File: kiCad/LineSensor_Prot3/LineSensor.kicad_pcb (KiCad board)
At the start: 2 copper layers, 146 parts, among them J1 Conn_01x04_Socket, J2 Conn_01x02_Socket, Q1 Q_Photo_NPN, Q10 Q_Photo_NPN, Q11 Q_Photo_NPN, Q12 Q_Photo_NPN, Q13 Q_Photo_NPN, Q14 Q_Photo_NPN, Q15 Q_Photo_NPN, Q16 Q_Photo_NPN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

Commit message: 円とセンサーの配置ずれるな..11/9
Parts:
- moved Q12 280.8 mm to (82.1, 177.8), turned to 157.5 degrees
- moved Q11 274.3 mm to (92.5, 162.2), turned to 135 degrees
- moved Q10 262.0 mm to (108.1, 151.8), turned to 112.5 degrees
- moved Q9 245.5 mm to (126.5, 148.2), turned to 90 degrees
- moved Q2 243.9 mm to (82.0, 214.5), turned to -157.5 degrees
- moved Q13 227.5 mm to (126.5, 244.2), turned to -90 degrees
- moved Q3 226.4 mm to (92.4, 230.1), turned to -135 degrees
- moved Q8 226.2 mm to (144.8, 151.8), turned to 67.5 degrees
- moved Q14 212.3 mm to (144.8, 240.5), turned to -67.5 degrees
- moved Q7 207.0 mm to (160.4, 162.2), turned to 45 degrees
- moved Q4 204.7 mm to (108.0, 240.5), turned to -112.5 degrees
- moved Q15 197.6 mm to (160.4, 230.1), turned to -45 degrees
- moved Q6 190.1 mm to (170.8, 177.8), turned to 22.5 degrees
- moved Q16 189.9 mm to (170.8, 214.5), turned to -22.5 degrees
- moved Q5 179.8 mm to (174.4, 196.2)
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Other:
- board text added: "ココ⇒"

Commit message: センサーフットプリント調整.11.9
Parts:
- removed D17: D, Diode_THT:D_DO-201AD_P12.70mm_Horizontal
- moved A1 230.2 mm to (427.4, 2.23)
- moved C10 230.2 mm to (428.2, 27.3)
- moved C2 230.2 mm to (419.7, 36.4)
- moved C3 230.2 mm to (410.3, 36.7)
- moved C4 230.2 mm to (428.2, 51.6)
- moved C5 230.2 mm to (428.2, 47.6)
- moved C7 230.2 mm to (428.2, 39.5)
- moved C8 230.2 mm to (428.2, 35.4)
- moved C9 230.2 mm to (428.2, 31.4)
- moved D18 230.2 mm to (352.4, -10.7)
- moved D19 230.2 mm to (349.8, -10.7)
- moved D20 230.2 mm to (347.2, -10.7)
- moved D21 230.2 mm to (344.6, -10.7)
- moved D22 230.2 mm to (342.0, -10.7)
- moved D23 230.2 mm to (339.5, -10.7)
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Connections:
- RV1 pad 2: Net-(U3A--) -> Net-(U3A-+)
- RV2 pad 2: Net-(U5A--) -> Net-(U5A-+)
- RV4 pad 2: Net-(U1A--) -> Net-(U1A-+)
- U1 pad 2: Net-(U1A--) -> Net-(Q13-E)
- U1 pad 3: Net-(Q13-E) -> Net-(U1A-+)
- U1 pad 5: Net-(Q14-E) -> Net-(U1A-+)
- U1 pad 6: Net-(U1A--) -> Net-(Q14-E)
- U2 pad 2: Net-(U1A--) -> Net-(Q15-E)
- U2 pad 3: Net-(Q15-E) -> Net-(U1A-+)
- U2 pad 5: Net-(Q16-E) -> Net-(U1A-+)
- U2 pad 6: Net-(U1A--) -> Net-(Q16-E)
- U3 pad 2: Net-(U3A--) -> Net-(Q1-E)
- U3 pad 3: Net-(Q1-E) -> Net-(U3A-+)
- U3 pad 5: Net-(Q2-E) -> Net-(U3A-+)
- U3 pad 6: Net-(U3A--) -> Net-(Q2-E)
- U4 pad 2: Net-(U3A--) -> Net-(Q3-E)
- U4 pad 3: Net-(Q3-E) -> Net-(U3A-+)
- U4 pad 5: Net-(Q4-E) -> Net-(U3A-+)
- U4 pad 6: Net-(U3A--) -> Net-(Q4-E)
- U5 pad 2: Net-(U5A--) -> Net-(Q12-E)
- U5 pad 3: Net-(Q12-E) -> Net-(U5A-+)
- U5 pad 5: Net-(Q11-E) -> Net-(U5A-+)
- U5 pad 6: Net-(U5A--) -> Net-(Q11-E)
- U6 pad 2: Net-(U5A--) -> Net-(Q10-E)
- U6 pad 3: Net-(Q10-E) -> Net-(U5A-+)
- U6 pad 5: Net-(Q9-E) -> Net-(U5A-+)
- U6 pad 6: Net-(U5A--) -> Net-(Q9-E)
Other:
- board text added: "300,200"

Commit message: 修学旅行行き新幹線
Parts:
- moved R67 479.4 mm to (63.9, 183.9)
- moved R12 477.8 mm to (49.9, 127.9)
- moved R13 477.8 mm to (49.9, 130.4)
- moved R14 477.8 mm to (49.9, 132.9)
- moved R15 477.8 mm to (49.9, 135.5)
- moved R16 477.8 mm to (49.9, 138.0)
- moved R17 477.8 mm to (49.9, 140.5)
- moved R18 477.8 mm to (49.9, 143.0)
- moved R19 477.8 mm to (49.9, 145.5)
- moved R20 477.8 mm to (49.9, 148.0)
- moved R21 477.8 mm to (49.9, 150.5)
- moved R22 477.8 mm to (49.9, 153.0)
- moved R45 477.8 mm to (63.0, 127.9)
- moved R46 477.8 mm to (63.0, 130.4)
- moved R47 477.8 mm to (63.0, 132.9)
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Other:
- board text removed: "300,200"
- board text removed: "ココ⇒"

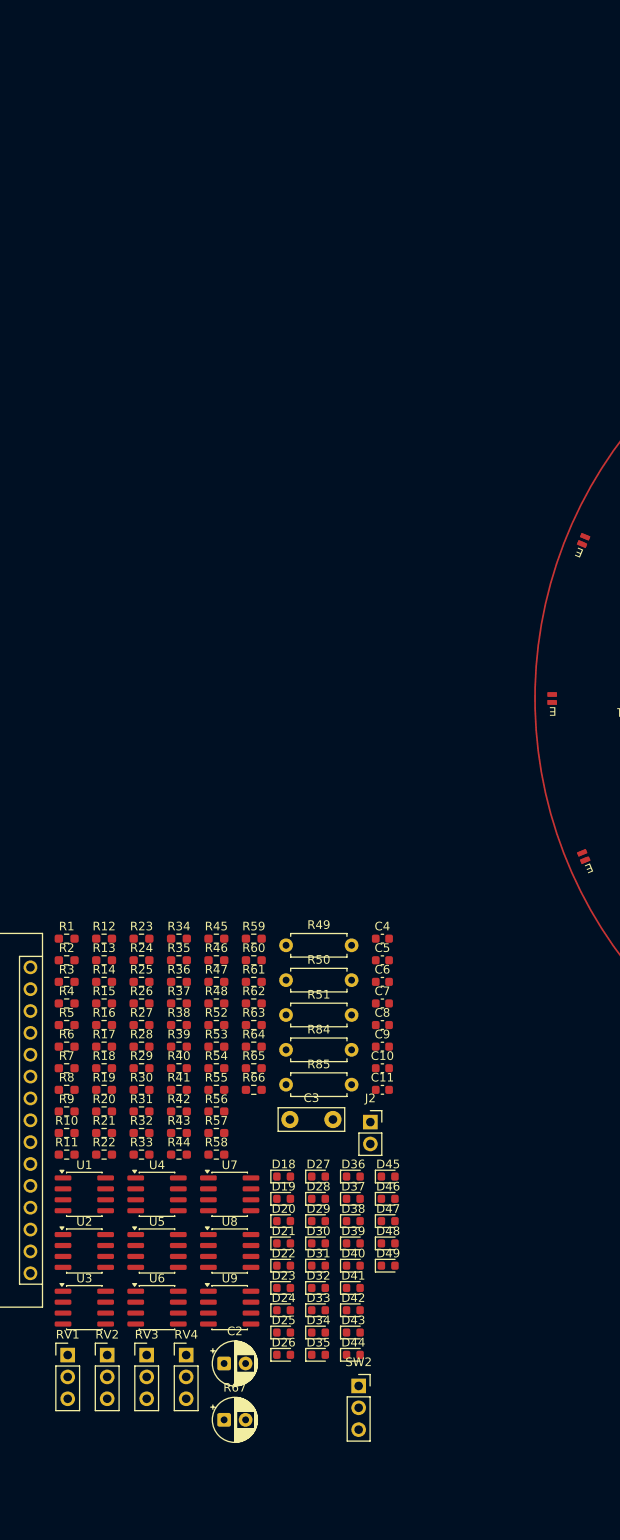
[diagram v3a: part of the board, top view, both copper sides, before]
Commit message: 11/1夜_LED配置まで
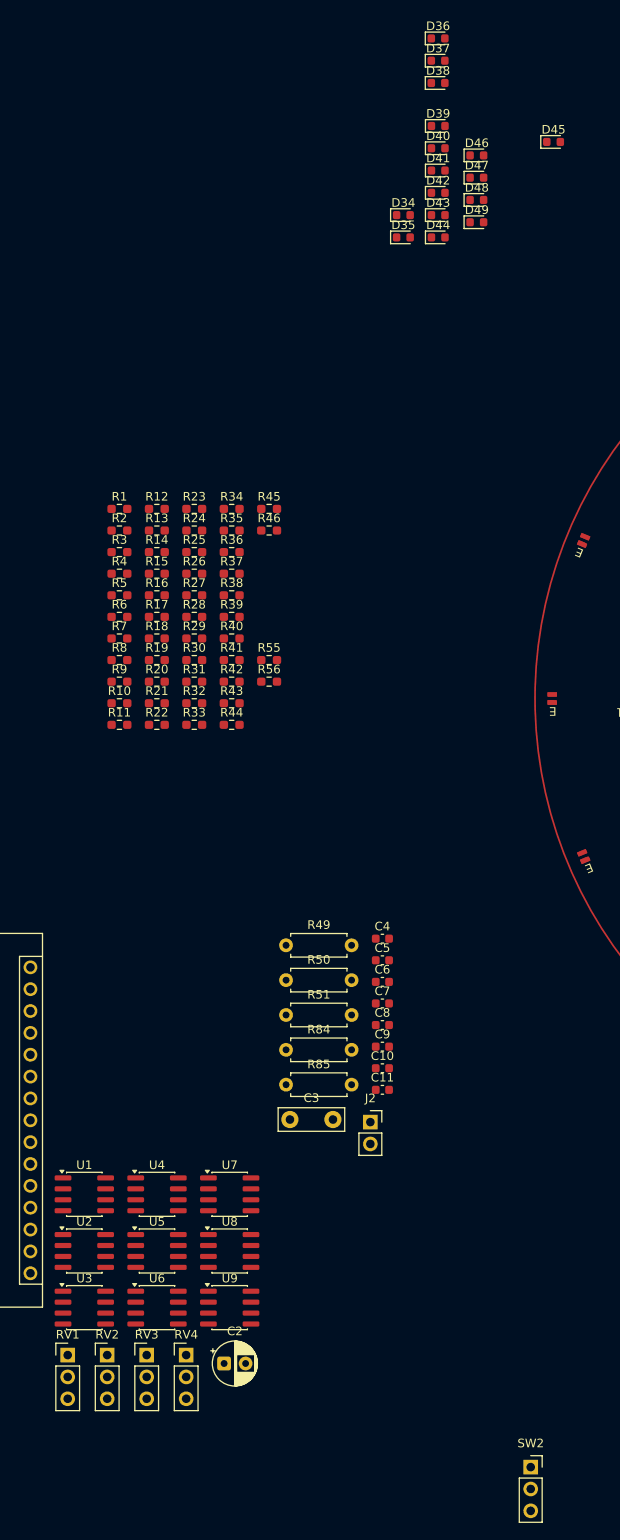
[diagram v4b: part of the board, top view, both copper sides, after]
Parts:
- removed D18, D19, D20, D21, D22, D23, D24, D25, D26, D27, D28, D29, D30, D31, D32, D33: LED, LED_SMD:LED_0603_1608Metric
- removed R47, R48, R52, R53, R54, R57, R58, R59, R60, R61, R62, R63, R64, R65, R66: R, Resistor_SMD:R_0603_1608Metric_Pad0.98x0.95mm_HandSolder
- removed R67: R, Capacitor_THT:CP_Radial_D5.0mm_P2.50mm
- moved D36 132.7 mm to (88.7, 23.3)
- moved D37 132.7 mm to (88.7, 25.9)
- moved D38 132.7 mm to (88.7, 28.5)
- moved D34 130.3 mm to (84.7, 43.8)
- moved D35 130.3 mm to (84.7, 46.4)
- moved D43 130.3 mm to (88.7, 43.8)
- moved D44 130.3 mm to (88.7, 46.4)
- moved D39 130.3 mm to (88.7, 33.5)
- moved D40 130.3 mm to (88.7, 36.1)
- moved D41 130.3 mm to (88.7, 38.6)
- moved D42 130.3 mm to (88.7, 41.2)
- moved D45 121.8 mm to (102.2, 35.3)
- moved D49 121.7 mm to (93.2, 44.7)
- moved D47 121.7 mm to (93.2, 39.5)
- moved D48 121.7 mm to (93.2, 42.1)
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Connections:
- D34 pad 1: unconnected-(D34-K-Pad1) -> Net-(D34-K)
- D36 pad 1: unconnected-(D36-K-Pad1) -> Net-(D36-K)
- D39 pad 1: unconnected-(D39-K-Pad1) -> Net-(D39-K)
- D40 pad 1: unconnected-(D40-K-Pad1) -> Net-(D40-K)
- R40 pad 1: unconnected-(R40-Pad1) -> Net-(D36-K)
- R43 pad 1: unconnected-(R43-Pad1) -> Net-(D39-K)
- R44 pad 1: unconnected-(R44-Pad1) -> Net-(D40-K)
- R55 pad 1: unconnected-(R55-Pad1) -> Net-(D34-K)

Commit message: 企画別行き
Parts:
- moved U1 154.6 mm to (187.2, 91.4)
- moved U2 142.8 mm to (182.0, 115.9)
- moved R13 139.7 mm to (194.8, 96.1), turned to -175 degrees
- moved R20 138.7 mm to (193.9, 113.8), turned to -17.5 degrees
- moved R14 133.9 mm to (189.9, 79.2), turned to 27.5 degrees
- moved R19 133.6 mm to (185.2, 129.6), turned to -40 degrees
- moved D34 131.1 mm to (181.8, 131.8), turned to 135 degrees
- moved D35 128.2 mm to (191.6, 117.2), turned to 157.5 degrees
- moved U7 125.8 mm to (163.3, 79.7)
- moved U8 125.8 mm to (163.3, 86.3)
- moved R15 125.3 mm to (179.6, 64.8), turned to 50 degrees
- moved R18 124.7 mm to (171.2, 140.8), turned to -62.5 degrees
- moved D45 124.5 mm to (166.9, 141.7), turned to 112 degrees
- moved U5 122.1 mm to (139.8, 75.5)
- moved U6 122.1 mm to (139.8, 82.0)
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
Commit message: LM393円形1
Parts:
- moved U1 58.8 mm to (160.5, 143.8), turned to -166.5 degrees
- moved R30 38.6 mm to (155.1, 126.9)
- moved R29 38.6 mm to (155.1, 124.4)
- moved U7 32.4 mm to (193.9, 90.3), turned to -77.5 degrees
- moved U3 30.1 mm to (106.3, 110.9), turned to 104 degrees
- moved U5 28.2 mm to (111.6, 76.5), turned to -121.5 degrees
- moved U8 26.8 mm to (173.2, 61.4), turned to -31 degrees
- moved U6 25.9 mm to (140.8, 56.2), turned to 13.5 degrees
- moved R22 20.0 mm to (148.7, 67.4)
- moved R21 20.0 mm to (148.7, 64.9)
- moved R5 19.4 mm to (137.9, 128.8)
- moved R6 19.4 mm to (137.9, 131.3)
- moved U4 16.1 mm to (126.5, 138.4), turned to 148.5 degrees
- moved R7 14.9 mm to (120.6, 106.2)
- moved R8 14.9 mm to (120.9, 110.9)
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
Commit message: 円形最低限
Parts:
- moved R36 132.6 mm to (195.6, 104.2), turned to -2 degrees
- moved R56 125.8 mm to (193.9, 113.8), turned to -17.5 degrees
- moved R35 125.4 mm to (190.1, 79.8), turned to 27.5 degrees
- moved R34 119.6 mm to (184.1, 70.1), turned to -140 degrees
- moved R37 118.2 mm to (169.3, 140.6), turned to -62.5 degrees
- moved R55 117.0 mm to (179.2, 135.1), turned to -48 degrees
- moved R33 113.5 mm to (164.3, 57.5), turned to 72.5 degrees
- moved R38 100.0 mm to (146.9, 144.9), turned to 85 degrees
- moved R40 97.4 mm to (154.4, 55.0), turned to 85 degrees
- moved R39 86.9 mm to (134.5, 142.4), turned to -107.5 degrees
- moved R41 75.3 mm to (130.8, 59.4), turned to 117.5 degrees
- moved R46 68.0 mm to (115.5, 130.2), turned to 40 degrees
- moved R42 64.2 mm to (120.5, 66.2), turned to -50 degrees
- moved R45 58.9 mm to (110.1, 120.3), turned to 35 degrees
- moved R43 45.7 mm to (107.6, 84.6), turned to 162.5 degrees
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
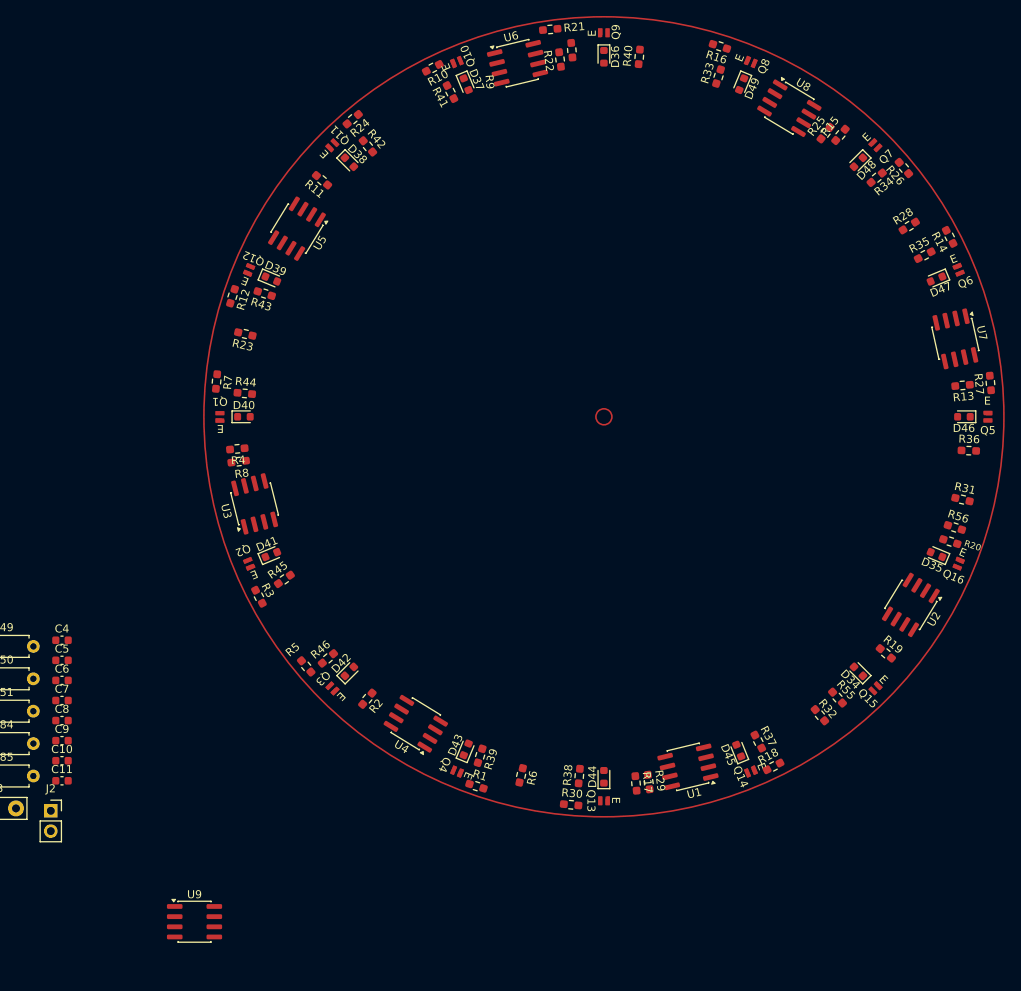
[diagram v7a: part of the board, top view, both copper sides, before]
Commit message: 円形配置 抵抗を平行に
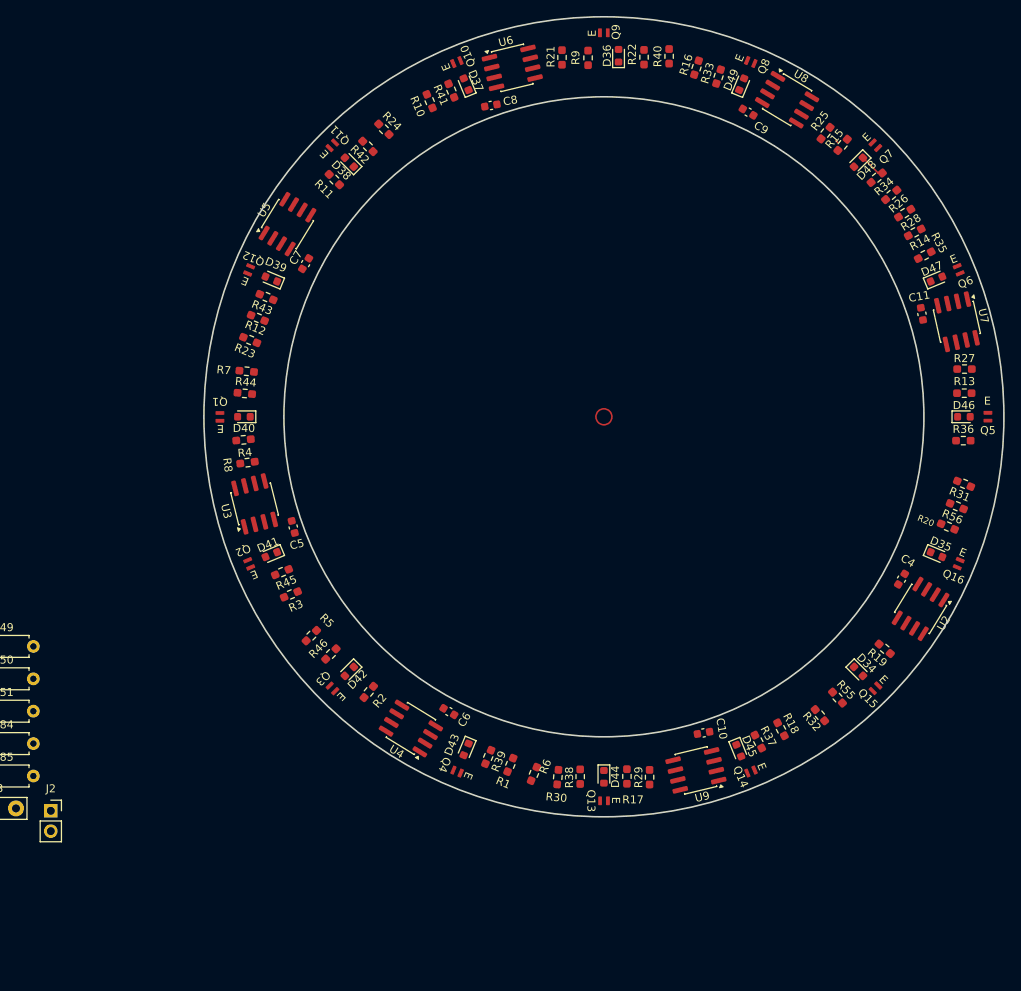
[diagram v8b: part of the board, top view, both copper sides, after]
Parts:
- removed U1: LM393, Package_SO:SOIC-8_3.9x4.9mm_P1.27mm
- moved C11 122.3 mm to (189.8, 87.1), turned to 100 degrees
- moved C9 116.3 mm to (168.0, 61.9), turned to -31 degrees
- moved C4 105.2 mm to (187.2, 120.3), turned to -121.5 degrees
- moved C8 93.7 mm to (135.9, 61.1), turned to 10 degrees
- moved C10 80.3 mm to (162.4, 139.5), turned to 10 degrees
- moved U9 65.5 mm to (161.5, 144.2), turned to -166.5 degrees
- moved C7 62.5 mm to (112.7, 80.9), turned to 58.5 degrees
- moved C6 48.5 mm to (130.6, 136.8), turned to 148.5 degrees
- moved C5 33.4 mm to (111.2, 113.8), turned to 104 degrees
- moved R22 10.5 mm to (155.0, 55.1), turned to -90 degrees
- moved R1 5.00 mm to (138.3, 143.5), turned to 67.5 degrees
- moved R18 4.73 mm to (172.1, 139.1), turned to 117.5 degrees
- moved R14 4.40 mm to (188.9, 76.9), turned to -152.5 degrees
- moved R10 4.18 mm to (128.2, 60.5), turned to -67.5 degrees
- moved R12 4.17 mm to (106.7, 87.6), turned to -22.5 degrees
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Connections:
- RV4 pad 2: Net-(U1A-+) -> Net-(U2A-+)
- U2 pad 3: Net-(U1A-+) -> Net-(U2A-+)
- U2 pad 4: VCC -> GND
- U2 pad 5: Net-(U1A-+) -> Net-(U2A-+)
- U2 pad 8: GND -> VCC
- U3 pad 4: VCC -> GND
- U3 pad 8: GND -> VCC
- U4 pad 4: VCC -> GND
- U4 pad 8: GND -> VCC
- U5 pad 4: VCC -> GND
- U5 pad 8: GND -> VCC
- U9 pad 1: (no net) -> Net-(A1-D11)
- U9 pad 2: (no net) -> Net-(U2A-+)
- U9 pad 3: (no net) -> Net-(Q13-E)
- U9 pad 5: (no net) -> Net-(Q14-E)
- U9 pad 6: (no net) -> Net-(U2A-+)
- U9 pad 7: (no net) -> Net-(A1-D12)
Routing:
- net Net-(D48-K): track 0.00 -> 3.21 mm
- net VCC: track 0.00 -> 0.60 mm
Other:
- board outline added: 100 x 100 mm
